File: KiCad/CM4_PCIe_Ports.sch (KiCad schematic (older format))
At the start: 3 parts, among them J13 10018783-11200TLF, J14 10018783-10113TLF, J15 10018783-10113TLF

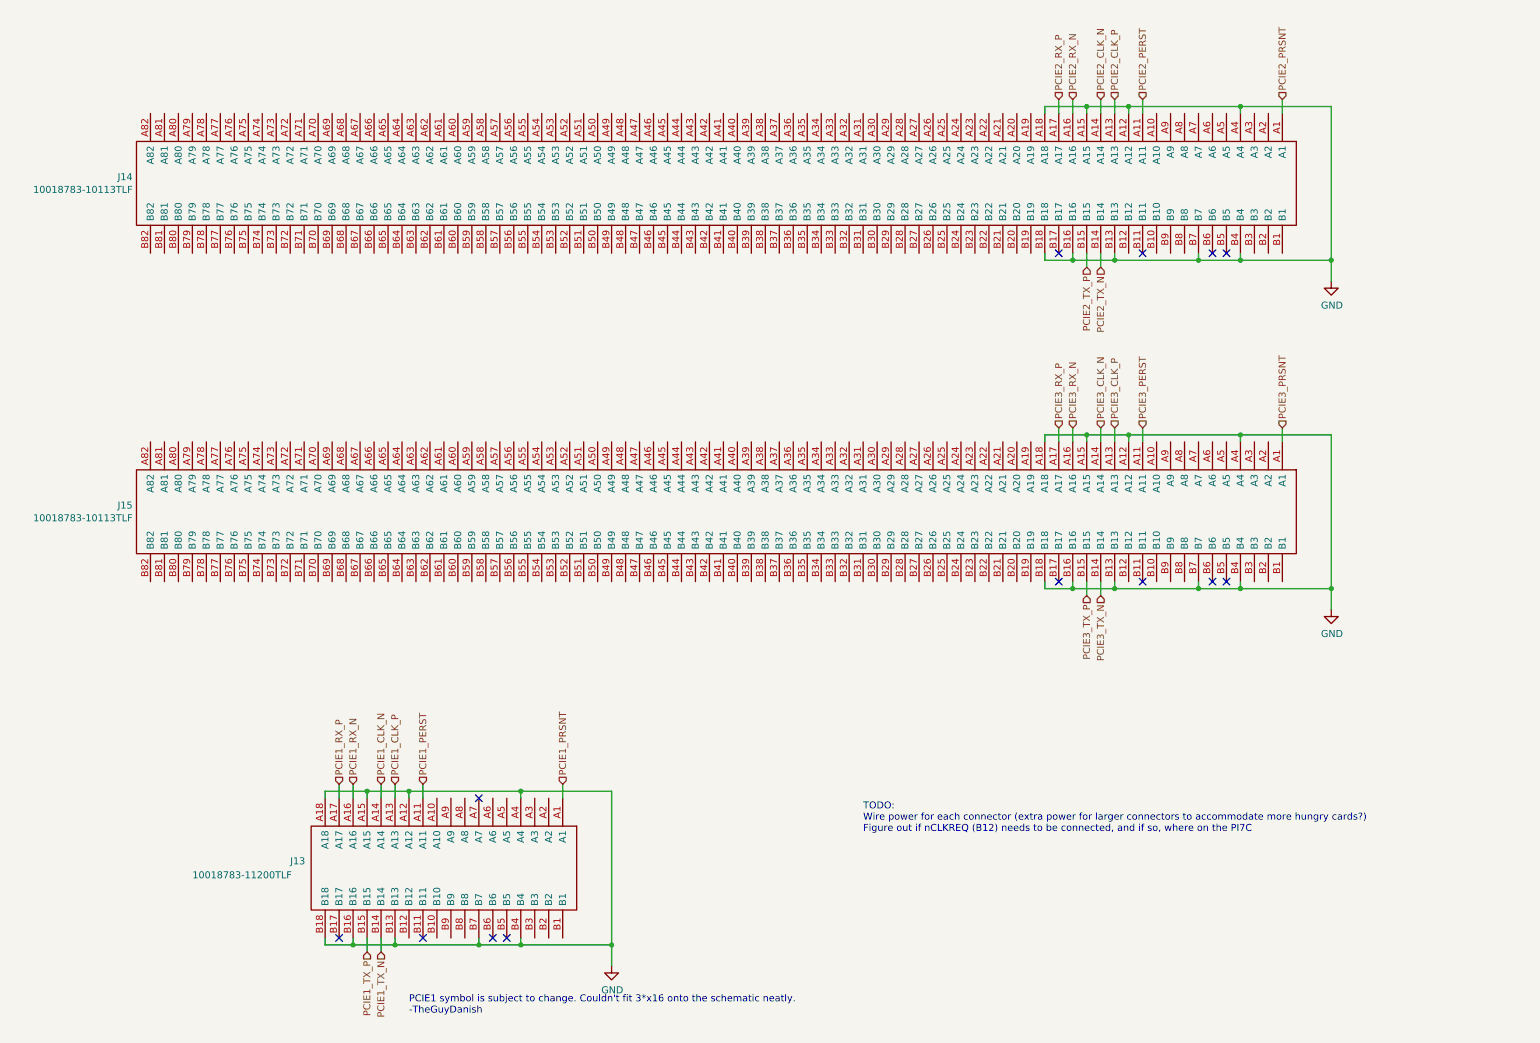
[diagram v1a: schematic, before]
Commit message: Small changes to PCIe, USB Schematics and board layout, legend for GPIO pins.
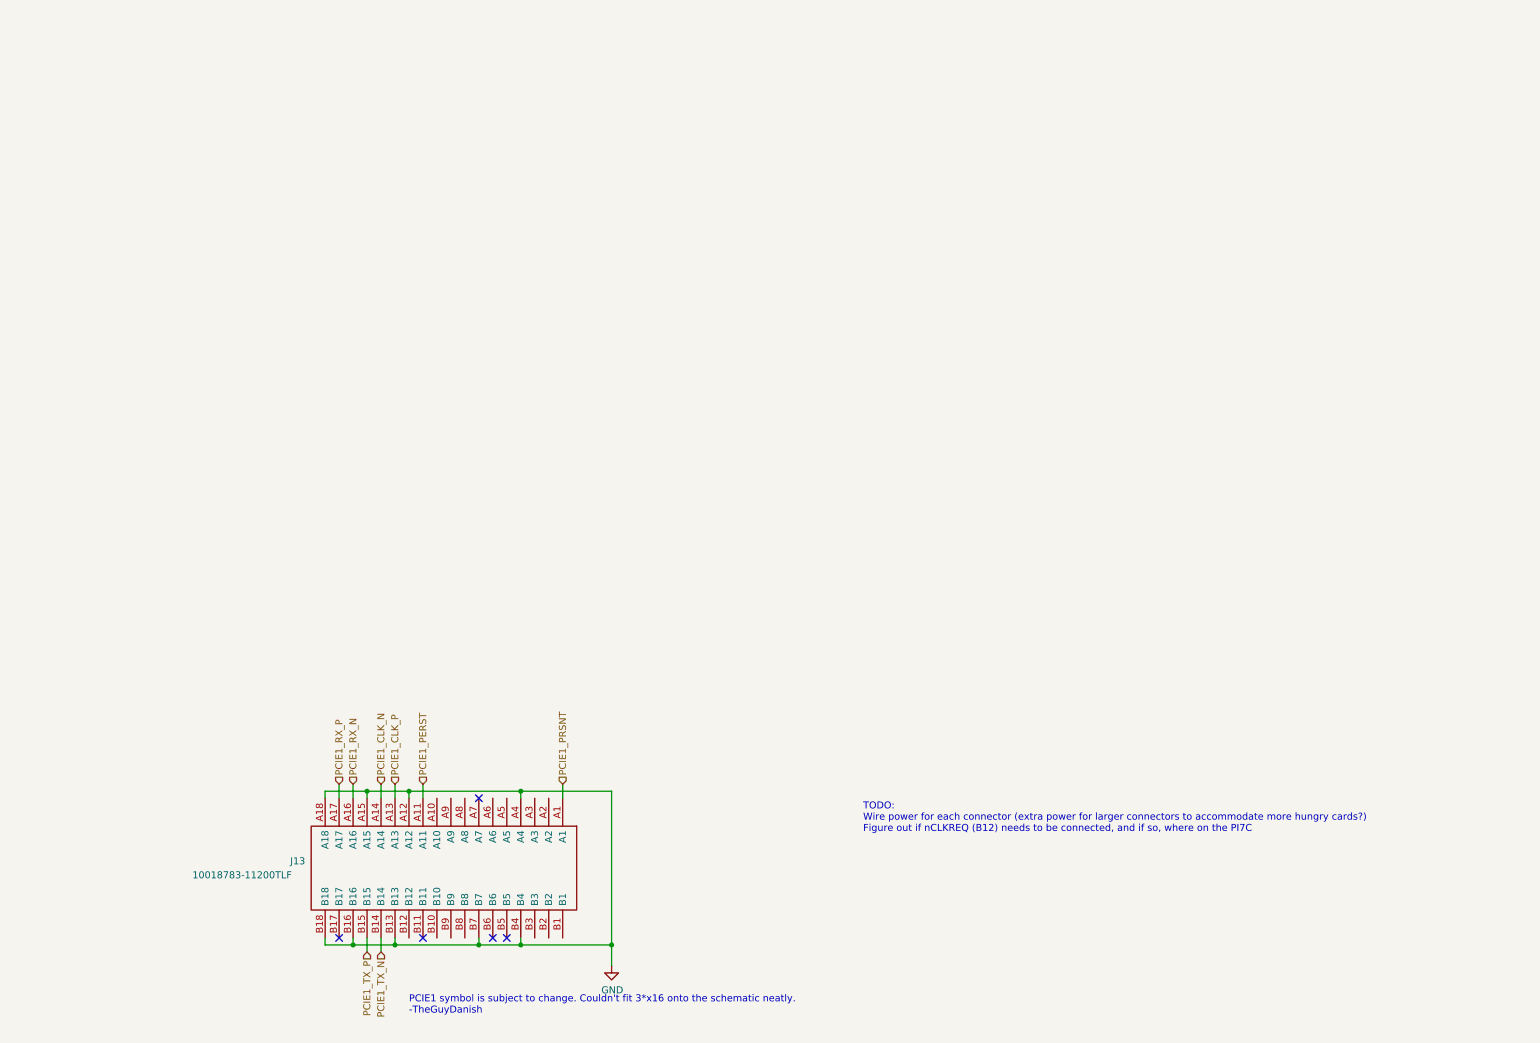
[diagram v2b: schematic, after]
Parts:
- removed J14: 10018783-10113TLF, CM4_MATX:10018783-10113TLF, symbol CM4_MATX:10018783-10113TLF
- removed J15: 10018783-10113TLF, 10018783-10113TLF, symbol CM4_MATX:10018783-10113TLF
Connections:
- no-connect marks 13 -> 5
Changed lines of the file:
@@
 $Descr A4 11693 8268
 encoding utf-8
-Sheet 6 8
+Sheet 6 10
 Title ""
 Date ""
@@
 Comment4 ""
 $EndDescr
-$Comp
-L CM4_MATX:10018783-10113TLF J14
-U 1 1 5FCA7C1E
-P 9950 1300
-F 0 "J14" V 10404 -6928 50  0000 R CNN
-F 1 "10018783-10113TLF" V 10495 -6928 50  0000 R CNN
-F 2 "CM4_MATX:10018783-10113TLF" H 10800 1400 50  0001 L CNN
-F 3 "" H 10800 1300 50  0001 L CNN
-F 4 "PCI Express / PCI Connectors x16 164 POS" H 10800 1200 50  0001 L CNN "Description"
-F 5 "649-18783-10113TLF" H 10800 1000 50  0001 L CNN "Mouser Part Number"
-F 6 "https://www.mouser.co.uk/ProductDetail/Amphenol-FCI/10018783-10113TLF?qs=9v8X2fPoQt7D6fmbE7fqDA%3D%3D" H 10800 900 50  0001 L CNN "Mouser Price/Stock"
-F 7 "Amphenol" H 10800 800 50  0001 L CNN "Manufacturer_Name"
-F 8 "10018783-10113TLF" H 10800 700 50  0001 L CNN "Manufacturer_Part_Number"
-	1    9950 1300
-	0    1    1    0
-$EndComp
-Text HLabel 9950 1200 1    50   Input ~ 0
-PCIE2_PRSNT
-Wire Wire Line
-	9950 1200 9950 1300
-Wire Wire Line
-	9650 1300 9650 1250
-Wire Wire Line
-	9650 1250 10300 1250
-Text HLabel 8950 1200 1    50   Input ~ 0
-PCIE2_PERST
-Wire Wire Line
-	8950 1200 8950 1300
-$Comp
-L power:GND #PWR0133
-U 1 1 5FCBA080
-P 10300 2500
-F 0 "#PWR0133" H 10300 2250 50  0001 C CNN
-F 1 "GND" H 10305 2327 50  0000 C CNN
-F 2 "" H 10300 2500 50  0001 C CNN
-F 3 "" H 10300 2500 50  0001 C CNN
-	1    10300 2500
-	1    0    0    -1
-$EndComp
-Wire Wire Line
-	10300 1250 10300 2350
-Wire Wire Line
-	9650 2300 9650 2350
-Wire Wire Line
-	9650 2350 10300 2350
-Connection ~ 10300 2350
-Wire Wire Line
-	10300 2350 10300 2500
-Wire Wire Line
-	8850 1300 8850 1250
-Wire Wire Line
-	8850 1250 9650 1250
-Connection ~ 9650 1250
-Text HLabel 8750 1200 1    50   Input ~ 0
-PCIE2_CLK_P
-Text HLabel 8650 1200 1    50   Input ~ 0
-PCIE2_CLK_N
-Wire Wire Line
-	8550 1300 8550 1250
-Wire Wire Line
-	8550 1250 8850 1250
-Connection ~ 8850 1250
-Text HLabel 8350 1200 1    50   Input ~ 0
-PCIE2_RX_P
-Text HLabel 8450 1200 1    50   Input ~ 0
-PCIE2_RX_N
-Wire Wire Line
-	8250 1300 8250 1250
-Wire Wire Line
-	8250 1250 8550 1250
-Connection ~ 8550 1250
-Wire Wire Line
-	8450 1300 8450 1200
-Wire Wire Line
-	8350 1200 8350 1300
-Wire Wire Line
-	8650 1200 8650 1300
-Wire Wire Line
-	8750 1300 8750 1200
-Wire Wire Line
-	9350 2300 9350 2350
-Wire Wire Line
-	9350 2350 9650 2350
-Connection ~ 9650 2350
-NoConn ~ 9450 2300
-NoConn ~ 9550 2300
-NoConn ~ 8950 2300
-Text HLabel 8650 2400 3    50   Input ~ 0
-PCIE2_TX_N
-Text HLabel 8550 2400 3    50   Input ~ 0
-PCIE2_TX_P
-Wire Wire Line
-	8550 2400 8550 2300
-Wire Wire Line
-	8650 2300 8650 2400
-Wire Wire Line
-	8750 2300 8750 2350
-Wire Wire Line
-	8750 2350 9350 2350
-Connection ~ 9350 2350
-Wire Wire Line
-	8450 2300 8450 2350
-Wire Wire Line
-	8450 2350 8750 2350
-Connection ~ 8750 2350
-Wire Wire Line
-	8250 2300 8250 2350
-Wire Wire Line
-	8250 2350 8450 2350
-Connection ~ 8450 2350
-NoConn ~ 8350 2300
-Wire Wire Line
-	8750 3550 8750 3650
-Wire Wire Line
-	8950 3550 8950 3650
-Wire Wire Line
-	9950 3650 9950 3550
-Wire Wire Line
-	8550 3600 8850 3600
-Connection ~ 8550 3600
-Wire Wire Line
-	8550 3650 8550 3600
-Wire Wire Line
-	8850 3600 9650 3600
-Connection ~ 8850 3600
-Wire Wire Line
-	8850 3600 8850 3650
-Wire Wire Line
-	9650 3600 10300 3600
-Connection ~ 9650 3600
-Wire Wire Line
-	9650 3650 9650 3600
-Wire Wire Line
-	8250 3600 8550 3600
-Wire Wire Line
-	8250 3650 8250 3600
-Text HLabel 9950 3550 1    50   Input ~ 0
-PCIE3_PRSNT
-Text HLabel 8950 3550 1    50   Input ~ 0
-PCIE3_PERST
-Text HLabel 8750 3550 1    50   Input ~ 0
-PCIE3_CLK_P
-Text HLabel 8650 3550 1    50   Input ~ 0
-PCIE3_CLK_N
-Text HLabel 8450 3550 1    50   Input ~ 0
-PCIE3_RX_N
-Text HLabel 8350 3550 1    50   Input ~ 0
-PCIE3_RX_P
-$Comp
-L CM4_MATX:10018783-10113TLF J15
-U 1 1 5FCD0EA6
-P 9950 3650
-F 0 "J15" V 10404 -4578 50  0000 R CNN
-F 1 "10018783-10113TLF" V 10495 -4578 50  0000 R CNN
-F 2 "10018783-10113TLF" H 10800 3750 50  0001 L CNN
-F 3 "" H 10800 3650 50  0001 L CNN
-F 4 "PCI Express / PCI Connectors x16 164 POS" H 10800 3550 50  0001 L CNN "Description"
-F 5 "649-18783-10113TLF" H 10800 3350 50  0001 L CNN "Mouser Part Number"
-F 6 "https://www.mouser.co.uk/ProductDetail/Amphenol-FCI/10018783-10113TLF?qs=9v8X2fPoQt7D6fmbE7fqDA%3D%3D" H 10800 3250 50  0001 L CNN "Mouser Price/Stock"
-F 7 "Amphenol" H 10800 3150 50  0001 L CNN "Manufacturer_Name"
-F 8 "10018783-10113TLF" H 10800 3050 50  0001 L CNN "Manufacturer_Part_Number"
-	1    9950 3650
-	0    1    1    0
-$EndComp
 $Comp
 L CM4_MATX:10018783-11200TLF J13
@@
 NoConn ~ 3800 7200
 NoConn ~ 4200 6200
-Wire Wire Line
-	10300 3600 10300 4700
-$Comp
-L power:GND #PWR0135
-U 1 1 5FD0EC2C
-P 10300 4850
-F 0 "#PWR0135" H 10300 4600 50  0001 C CNN
-F 1 "GND" H 10305 4677 50  0000 C CNN
-F 2 "" H 10300 4850 50  0001 C CNN
-F 3 "" H 10300 4850 50  0001 C CNN
-	1    10300 4850
-	1    0    0    -1
-$EndComp
-Wire Wire Line
-	9650 4700 9650 4650
-Wire Wire Line
-	9350 4650 9350 4700
-Wire Wire Line
-	9350 4700 9650 4700
-Wire Wire Line
-	9650 4700 10300 4700
-Connection ~ 9650 4700
-Connection ~ 10300 4700
-Wire Wire Line
-	10300 4700 10300 4850
-Wire Wire Line
-	9350 4700 8750 4700
-Wire Wire Line
-	8750 4700 8750 4650
-Connection ~ 9350 4700
-Wire Wire Line
-	8750 4700 8450 4700
-Wire Wire Line
-	8450 4700 8450 4650
-Connection ~ 8750 4700
-Wire Wire Line
-	8450 4700 8250 4700
-Wire Wire Line
-	8250 4700 8250 4650
-Connection ~ 8450 4700
-Wire Wire Line
-	8650 3650 8650 3550
-Wire Wire Line
-	8450 3550 8450 3650
-Wire Wire Line
-	8350 3650 8350 3550
-Text HLabel 8550 4750 3    50   Input ~ 0
-PCIE3_TX_P
-Text HLabel 8650 4750 3    50   Input ~ 0
-PCIE3_TX_N
-Wire Wire Line
-	8650 4750 8650 4650
-Wire Wire Line
-	8550 4650 8550 4750
-NoConn ~ 8350 4650
-NoConn ~ 8950 4650
-NoConn ~ 9450 4650
-NoConn ~ 9550 4650
 Text Notes 3700 7750 0    50   ~ 0
 PCIE1 symbol is subject to change. Couldn't fit 3*x16 onto the schematic neatly.\n-TheGuyDanish
